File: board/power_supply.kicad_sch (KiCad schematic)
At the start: 8 parts, among them J1 Barrel_Jack, U1 NCP1117ST33T3G, U2 NCP1117ST50T3G

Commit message: finish board design
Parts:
- added NT301, NT302: NetTie_2, NetTie:NetTie-2_SMD_Pad0.5mm, symbol Device:NetTie_2
- renumbered C1 to C301, C2 to C302, C3 to C303, C4 to C304, J1 to J301, U1 to U301, U2 to U302
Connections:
- net +3.3V: now also NT301.2; no longer C302.1, U301.2 (VO)
- net +5V: now also NT302.2; no longer C304.1, U302.2 (VO)
- new net: C304.1, NT302.1, U302.2 (VO)
- new net: C302.1, NT301.1, U301.2 (VO)

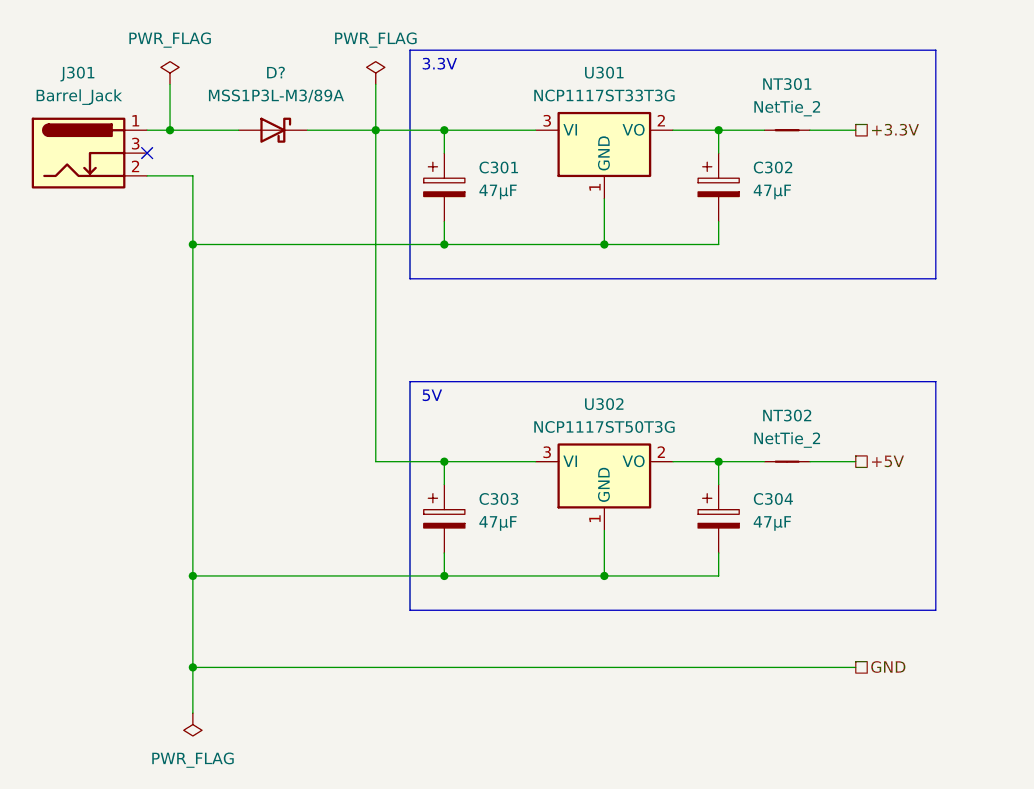
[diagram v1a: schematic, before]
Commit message: redo board to use I2C port expanders (and smaller MCU)
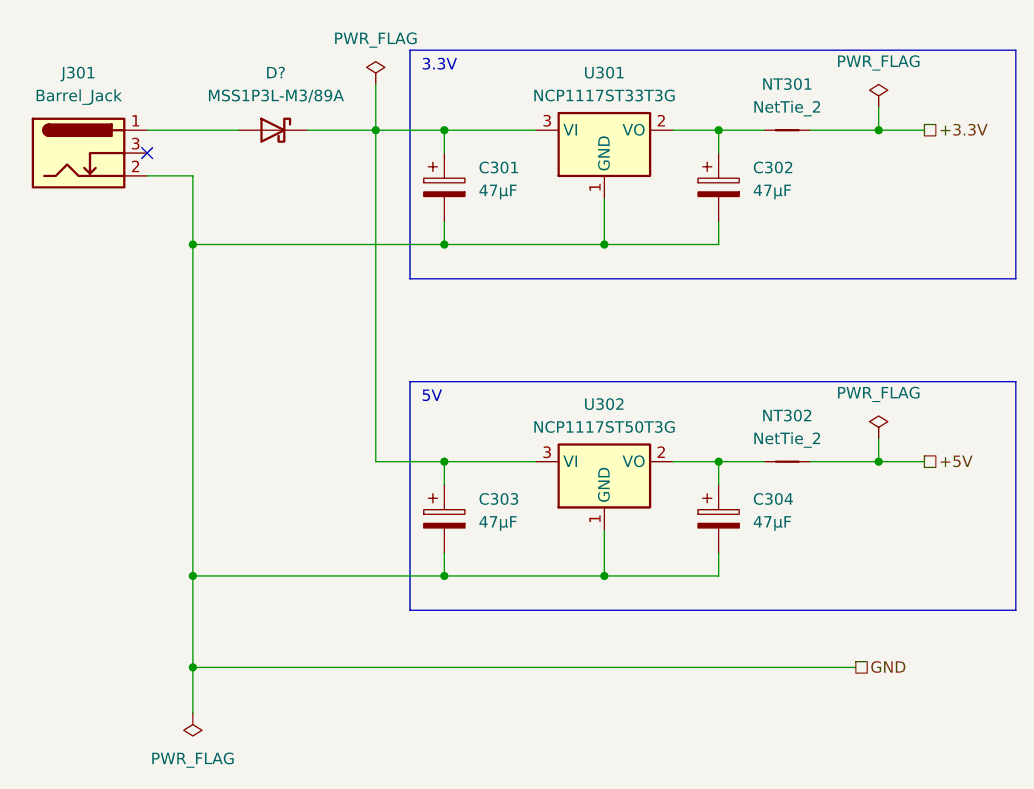
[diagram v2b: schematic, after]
